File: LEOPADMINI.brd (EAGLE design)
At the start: 54 x 83 mm, 47 parts, among them IC1 ATMEGA32U4-QFN

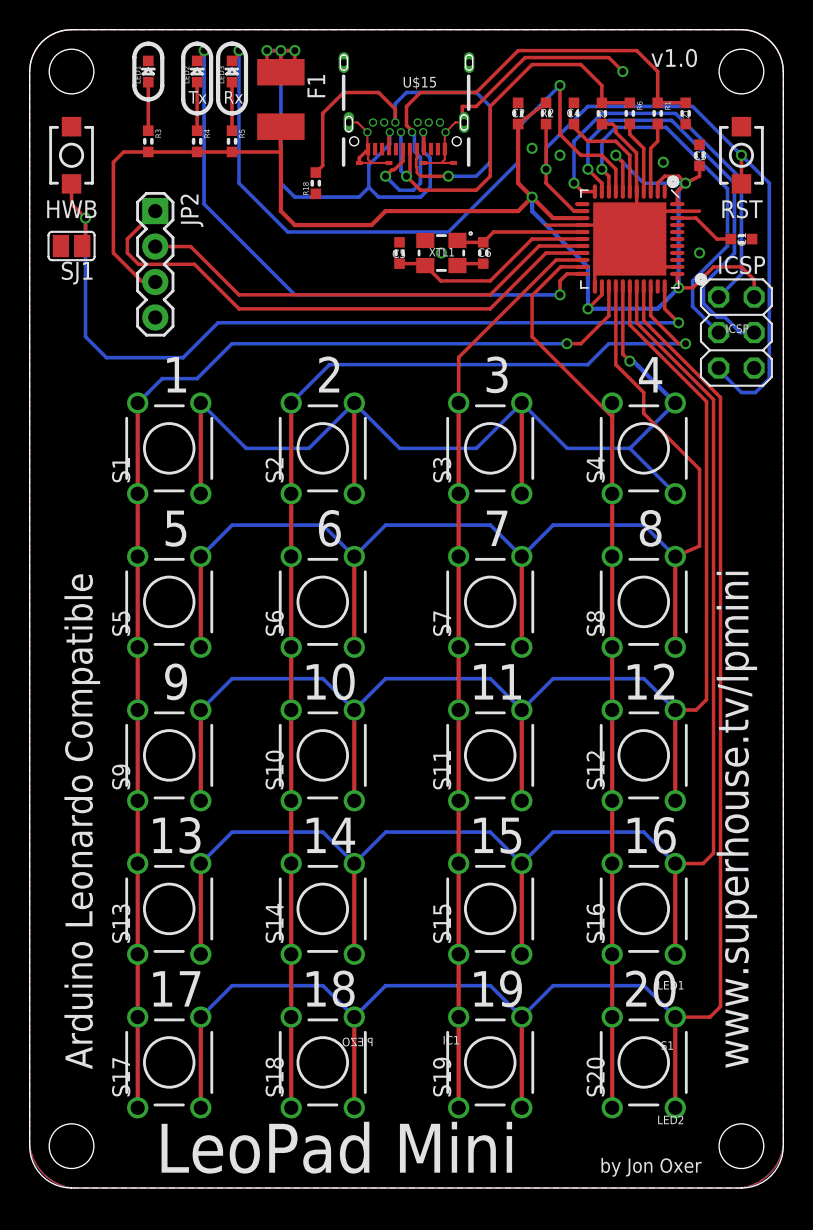
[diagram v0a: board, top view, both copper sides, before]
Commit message: Fixed button spacing for v1.0 release
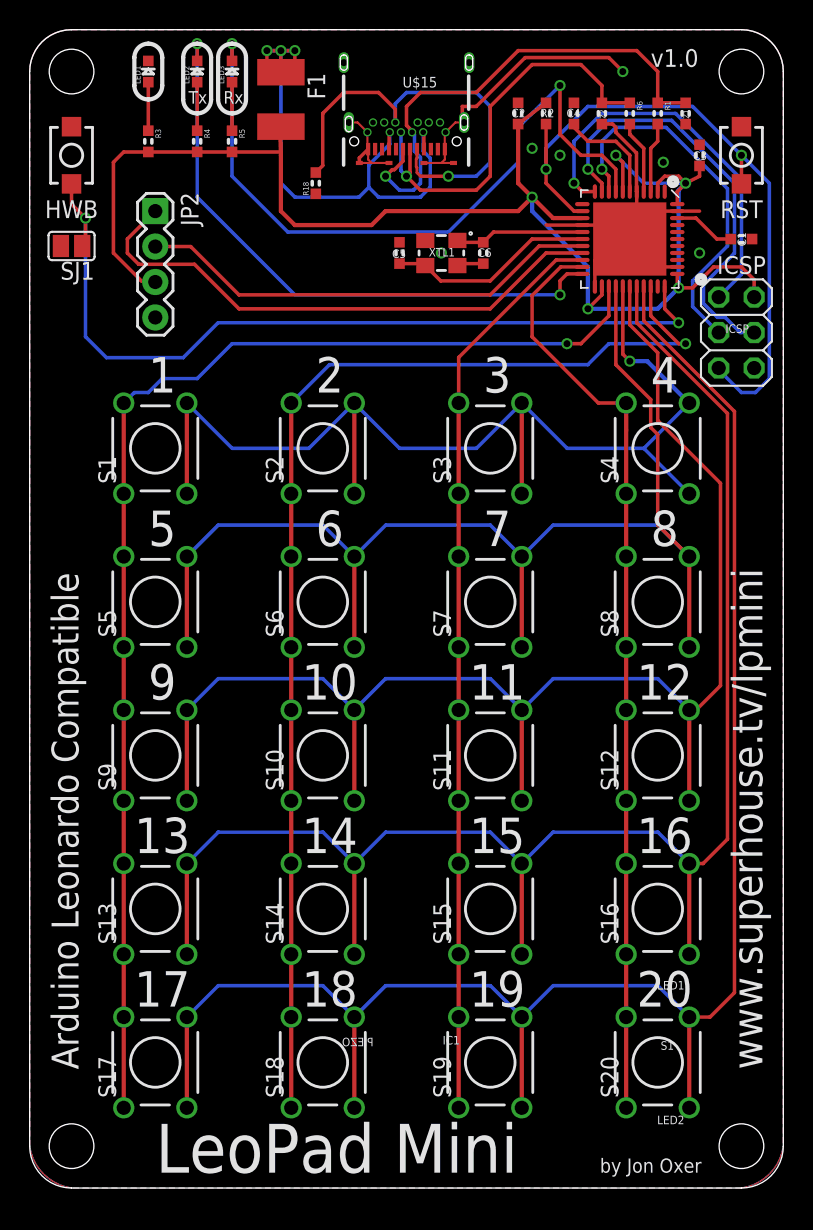
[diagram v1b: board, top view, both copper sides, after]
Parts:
- moved S1 1.00 mm to (9.00, 53.0)
- moved S12 1.00 mm to (45.0, 31.0)
- moved S13 1.00 mm to (9.00, 20.0)
- moved S16 1.00 mm to (45.0, 20.0)
- moved S17 1.00 mm to (9.00, 9.00)
- moved S20 1.00 mm to (45.0, 9.00)
- moved S4 1.00 mm to (45.0, 53.0)
- moved S5 1.00 mm to (9.00, 42.0)
- moved S8 1.00 mm to (45.0, 42.0)
- moved S9 1.00 mm to (9.00, 31.0)
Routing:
- net ROW0: track 76.2 -> 79.2 mm
- net ROW4: track 123.0 -> 124.9 mm
- net ROW3: track 111.5 -> 113.4 mm
- net ROW2: track 100.0 -> 101.9 mm
- net COL3: track 67.0 -> 68.6 mm
- net COL0: track 88.9 -> 89.9 mm
- net RXLED_SS: track 51.2 -> 51.8 mm
- net TX_LED: track 43.3 -> 43.9 mm
- net ROW1: track 88.6 -> 89.1 mm

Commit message: Improved designator positions
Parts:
- C1, C2: value 100nF 0603 -> 100nF
- C3, C4: value 1uF 0603 -> 1uF
- C5, C6: value 15pF 0603 -> 15pF
- R2: value 10K 0603 -> 10K

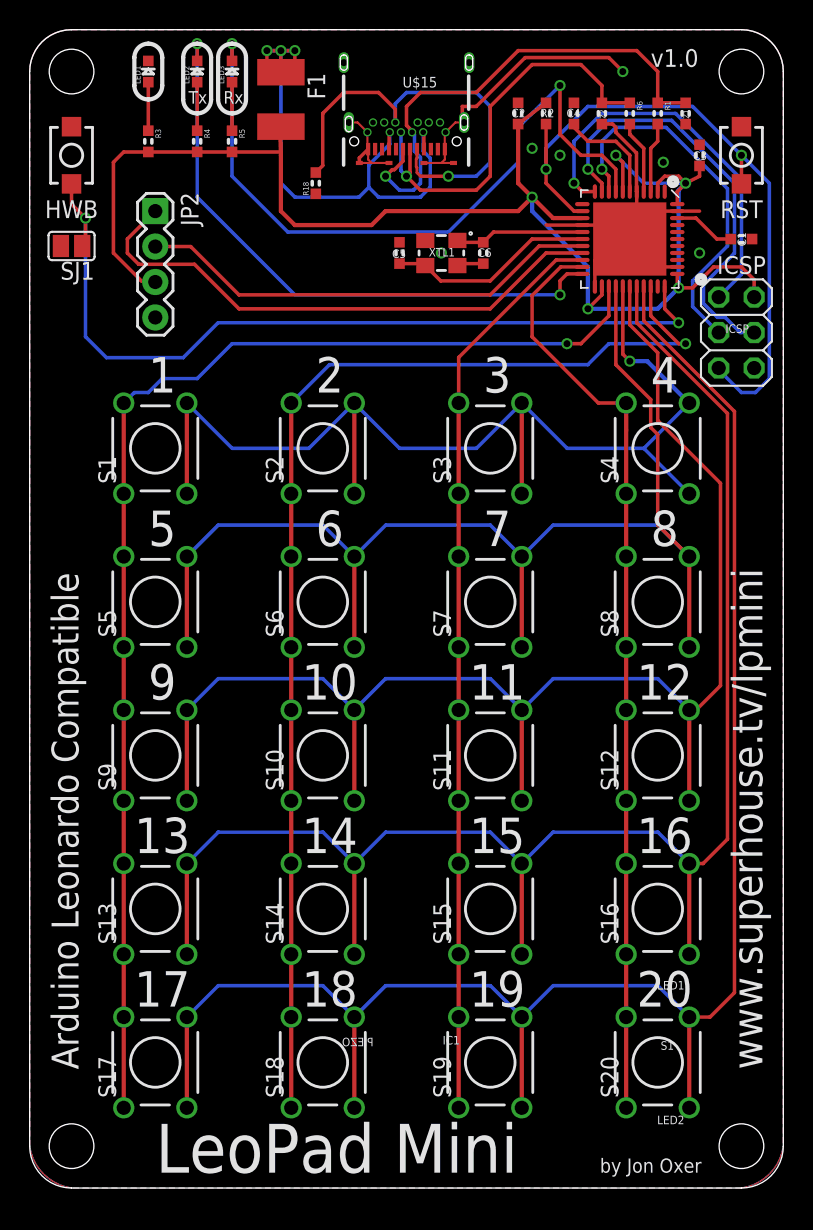
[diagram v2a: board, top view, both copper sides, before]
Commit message: Replaced most parts using SuperHouse library to add 3D models
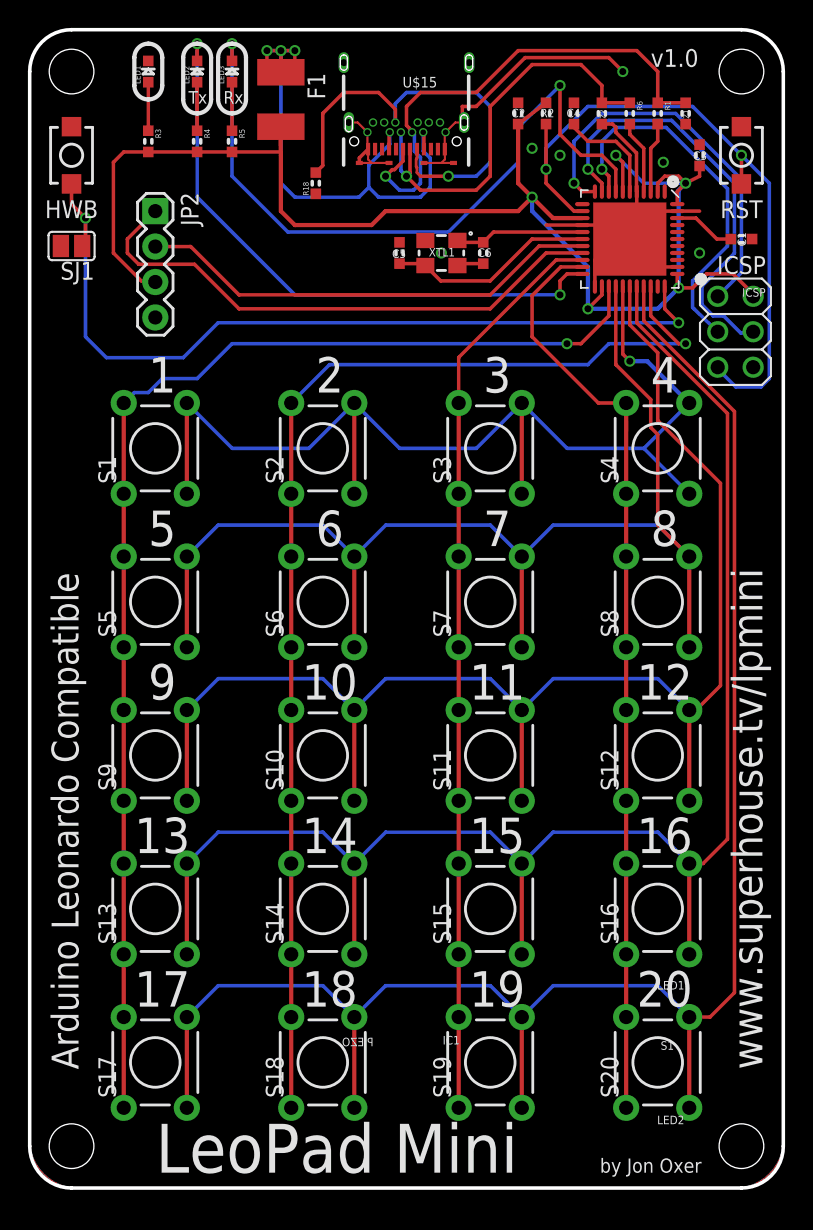
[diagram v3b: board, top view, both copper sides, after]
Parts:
- ICSP: device pinhead:2X03 -> SuperHouse-Connectors:2X03PTH
- S1, S10, S11, S12, S13, S14, S15, S16, S17, S18, S19, S2, S20, S3, S4, S5, S6, S7, S8, S9: device freetronics-original:TACTILE-PTH -> SuperHouse-Switches:TACTILE-PTH-6MM
- moved ICSP 2.86 mm to (51.8, 63.9)
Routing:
- net 5V: track 111.1 -> 109.9 mm

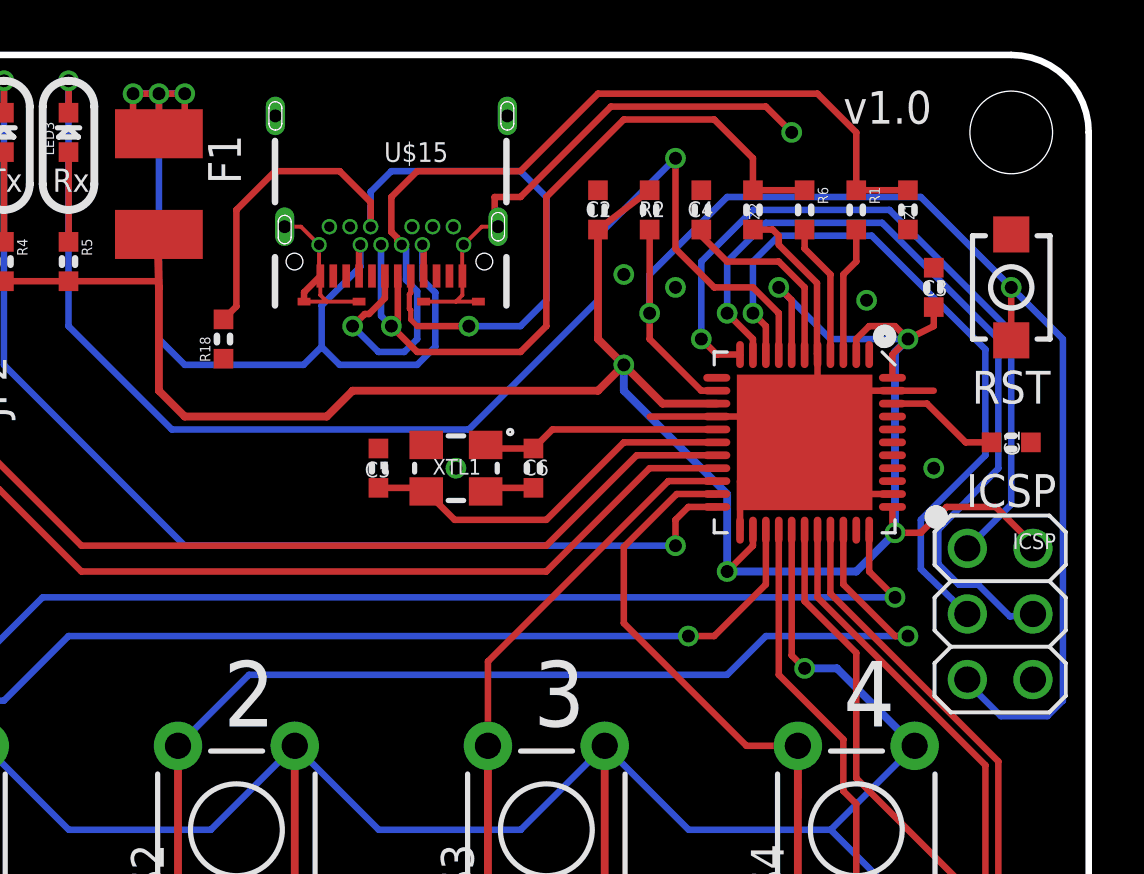
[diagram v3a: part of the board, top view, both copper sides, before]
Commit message: Replaced parts using SuperHouse library to add 3D models
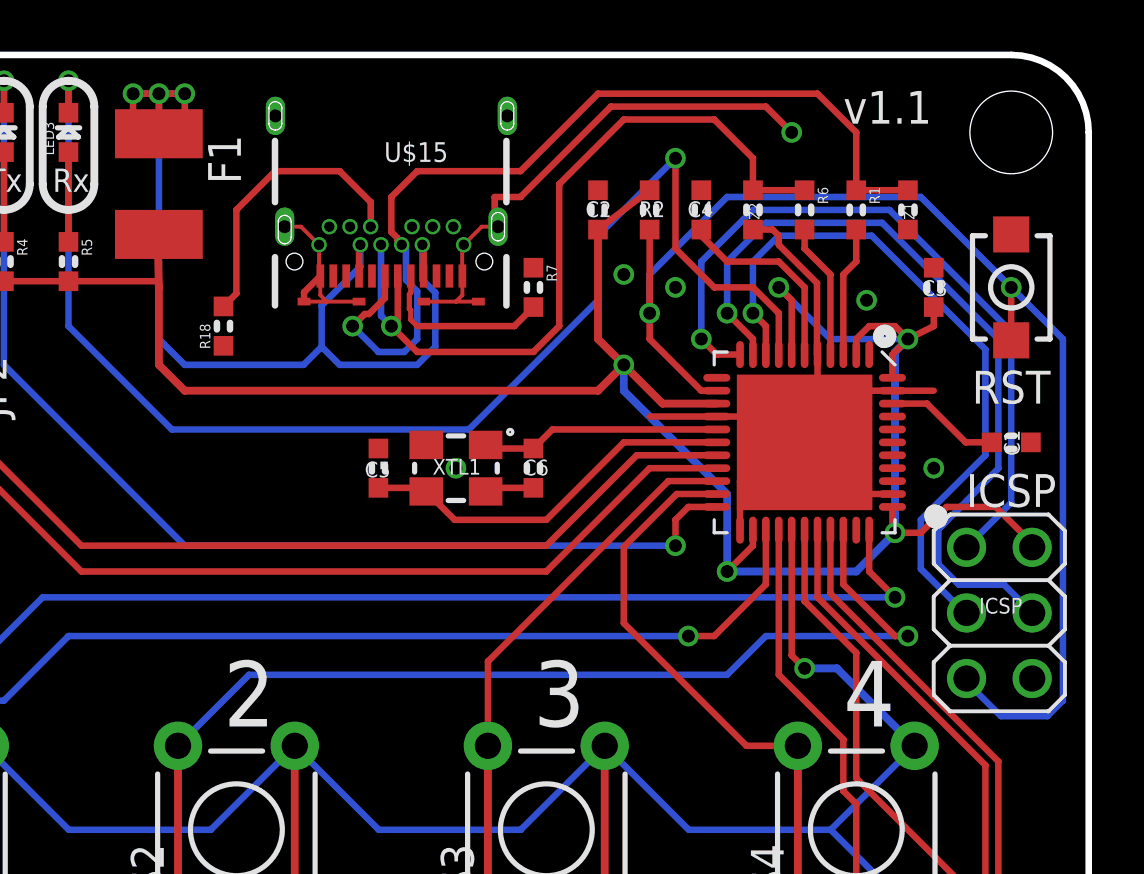
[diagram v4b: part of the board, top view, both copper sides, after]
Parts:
- added R7: 5.1K, SuperHouse-DiscreteSemi:R0603
- C1, C2, C3, C4, C5, C6: device freetronics-master-v1.1:0603 -> SuperHouse-DiscreteSemi:C0603
- F1: device rcl:L1812 -> SuperHouse-Fuses:1812
- LED1, LED2, LED3: device freetronics-jon:LED-0603 -> SuperHouse-LEDs:LED-0603
- R1, R3, R4, R5, R6: device freetronics-jon:0603 -> SuperHouse-DiscreteSemi:R0603
- R18: device freetronics-original:0603 -> SuperHouse-DiscreteSemi:R0603
- R2: device freetronics-master-v1.1:0603 -> SuperHouse-DiscreteSemi:R0603
- S21, S22: device freetronics-jon:TACTILE_SWITCH_SMD_2PIN_TINY -> SuperHouse-Switches:TACTILE_SMD_3X4X2
- U$15: device freetronics-jon:USB-C-U52A -> SuperHouse-Connectors:USB-C-U52A
- XTL1: device freetronics-jon:CRYSTAL-SMD-3X2 -> SuperHouse-Oscillators:CRYSTAL-SMD-3X2
- Z1, Z2: device freetronics-master-v1.1:0603 -> SuperHouse-DiscreteSemi:TVS0603
- moved ICSP 2.82 mm to (50.5, 61.4)
- moved R18 0.50 mm to (20.5, 72.5)
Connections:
- new net N$1: R18.2, U$15.B5
- net GND: now also R7.1
- net N$67: now also R7.2; no longer R18.2, U$15.B5
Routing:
- net N$67: track 32.1 -> 6.89 mm, vias 1 -> 0
- net N$1: track 0.00 -> 11.2 mm
- net 5V: track 109.9 -> 108.9 mm
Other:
- board text added: "v1.1"
- board text removed: "v1.0"
